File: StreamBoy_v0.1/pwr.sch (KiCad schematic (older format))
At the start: 4 parts

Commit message: Bunch of stuff
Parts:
- removed C1: 22uF/25V, Capacitor_SMD:C_0805_2012Metric, symbol Device:C
- removed C2: 0.1uF/50V, Capacitor_SMD:C_0805_2012Metric, symbol Device:C
- added C4, C? (x2): C, Capacitor_SMD:C_0805_2012Metric, symbol Device:C
- added D1, D2: D_Zener, b240a-13-f:DIOM5136X261N, symbol Device:D_Zener
- added L1, L2: INDUCTOR, Inductor_SMD:L_0805_2012Metric, symbol pspice:INDUCTOR
- added R43, R? (x3): R, Resistor_SMD:R_0805_2012Metric, symbol Device:R
- added U5, U6: TPS62170DSG, Package_SON:WSON-8-1EP_2x2mm_P0.5mm_EP0.9x1.6mm_ThermalVias, symbol Regulator_Switching:TPS62170DSG
- C3: value 0.1uF/50V -> C
- R1: value 10k -> R
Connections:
- net labels removed: GND
- wire segments 14 -> 0
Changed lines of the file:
@@
 Comment4 ""
 $EndDescr
+Text GLabel 9000 1550 2    50   Input ~ 0
+VCC3
+Text GLabel 9150 1950 2    50   Input ~ 0
+ESP_EN
 $Comp
-L Device:C C1
-U 1 1 5E0A08F0
-P 1550 1600
-F 0 "C1" H 1665 1646 50  0000 L CNN
-F 1 "22uF/25V" H 1665 1555 50  0000 L CNN
-F 2 "Capacitor_SMD:C_0805_2012Metric" H 1588 1450 50  0001 C CNN
-F 3 "~" H 1550 1600 50  0001 C CNN
-	1    1550 1600
+L Regulator_Switching:TPS62170DSG U6
+U 1 1 5E088ABF
+P 6900 1950
+F 0 "U6" H 6900 2517 50  0000 C CNN
+F 1 "TPS62170DSG" H 6900 2426 50  0000 C CNN
+F 2 "Package_SON:WSON-8-1EP_2x2mm_P0.5mm_EP0.9x1.6mm_ThermalVias" H 7050 1600 50  0001 L CNN
+F 3 "http://www.ti.com/lit/ds/symlink/tps62170.pdf" H 6900 2500 50  0001 C CNN
+	1    6900 1950
 	1    0    0    -1
 $EndComp
 $Comp
-L Device:C C2
-U 1 1 5E0A08F6
-P 1850 1400
-F 0 "C2" H 1965 1446 50  0000 L CNN
-F 1 "0.1uF/50V" H 1965 1355 50  0000 L CNN
-F 2 "Capacitor_SMD:C_0805_2012Metric" H 1888 1250 50  0001 C CNN
-F 3 "~" H 1850 1400 50  0001 C CNN
-	1    1850 1400
+L Regulator_Switching:TPS62170DSG U5
+U 1 1 5E08B4BD
+P 6850 3150
+F 0 "U5" H 6850 3717 50  0000 C CNN
+F 1 "TPS62170DSG" H 6850 3626 50  0000 C CNN
+F 2 "Package_SON:WSON-8-1EP_2x2mm_P0.5mm_EP0.9x1.6mm_ThermalVias" H 7000 2800 50  0001 L CNN
+F 3 "http://www.ti.com/lit/ds/symlink/tps62170.pdf" H 6850 3700 50  0001 C CNN
+	1    6850 3150
+	1    0    0    -1
+$EndComp
+$Comp
+L Device:D_Zener D1
+U 1 1 5E08BEF3
+P 5050 1750
+F 0 "D1" H 5050 1966 50  0000 C CNN
+F 1 "D_Zener" H 5050 1875 50  0000 C CNN
+F 2 "b240a-13-f:DIOM5136X261N" H 5050 1750 50  0001 C CNN
+F 3 "~" H 5050 1750 50  0001 C CNN
+	1    5050 1750
+	1    0    0    -1
+$EndComp
+$Comp
+L Device:D_Zener D2
+U 1 1 5E08C9DF
+P 5050 2150
+F 0 "D2" H 5050 2366 50  0000 C CNN
+F 1 "D_Zener" H 5050 2275 50  0000 C CNN
+F 2 "b240a-13-f:DIOM5136X261N" H 5050 2150 50  0001 C CNN
+F 3 "~" H 5050 2150 50  0001 C CNN
+	1    5050 2150
 	1    0    0    -1
 $EndComp
 $Comp
 L Device:C C3
-U 1 1 5E0A08FC
-P 2450 1950
-F 0 "C3" H 2565 1996 50  0000 L CNN
-F 1 "0.1uF/50V" H 2565 1905 50  0000 L CNN
-F 2 "Capacitor_SMD:C_0805_2012Metric" H 2488 1800 50  0001 C CNN
-F 3 "~" H 2450 1950 50  0001 C CNN
-	1    2450 1950
+U 1 1 5E08EF4C
+P 5600 2600
+F 0 "C3" H 5715 2646 50  0000 L CNN
+F 1 "C" H 5715 2555 50  0000 L CNN
+F 2 "Capacitor_SMD:C_0805_2012Metric" H 5638 2450 50  0001 C CNN
+F 3 "~" H 5600 2600 50  0001 C CNN
+	1    5600 2600
+	1    0    0    -1
+$EndComp
+$Comp
+L Device:C C4
+U 1 1 5E08F357
+P 5600 3300
+F 0 "C4" H 5715 3346 50  0000 L CNN
+F 1 "C" H 5715 3255 50  0000 L CNN
+F 2 "Capacitor_SMD:C_0805_2012Metric" H 5638 3150 50  0001 C CNN
+F 3 "~" H 5600 3300 50  0001 C CNN
+	1    5600 3300
+	1    0    0    -1
+$EndComp
+$Comp
+L Device:R R43
+U 1 1 5E08FF72
+P 5550 4100
+F 0 "R43" H 5620 4146 50  0000 L CNN
+F 1 "R" H 5620 4055 50  0000 L CNN
+F 2 "Resistor_SMD:R_0805_2012Metric" V 5480 4100 50  0001 C CNN
+F 3 "~" H 5550 4100 50  0001 C CNN
+	1    5550 4100
 	1    0    0    -1
 $EndComp
 $Comp
 L Device:R R1
-U 1 1 5E0A0902
-P 2450 1400
-F 0 "R1" H 2520 1446 50  0000 L CNN
-F 1 "10k" H 2520 1355 50  0000 L CNN
-F 2 "Resistor_SMD:R_0805_2012Metric" V 2380 1400 50  0001 C CNN
-F 3 "~" H 2450 1400 50  0001 C CNN
-	1    2450 1400
+U 1 1 5E09032D
+P 5300 4100
+F 0 "R1" H 5370 4146 50  0000 L CNN
+F 1 "R" H 5370 4055 50  0000 L CNN
+F 2 "Resistor_SMD:R_0805_2012Metric" V 5230 4100 50  0001 C CNN
+F 3 "~" H 5300 4100 50  0001 C CNN
+	1    5300 4100
 	1    0    0    -1
 $EndComp
 $Comp
-L power:GND #PWR0101
-U 1 1 5E0A0908
-P 1550 2200
-F 0 "#PWR0101" H 1550 1950 50  0001 C CNN
-F 1 "GND" H 1555 2027 50  0000 C CNN
-F 2 "" H 1550 2200 50  0001 C CNN
-F 3 "" H 1550 2200 50  0001 C CNN
-	1    1550 2200
+L pspice:INDUCTOR L1
+U 1 1 5E0929E5
+P 8600 1800
+F 0 "L1" H 8600 2015 50  0000 C CNN
+F 1 "INDUCTOR" H 8600 1924 50  0000 C CNN
+F 2 "Inductor_SMD:L_0805_2012Metric" H 8600 1800 50  0001 C CNN
+F 3 "~" H 8600 1800 50  0001 C CNN
+	1    8600 1800
 	1    0    0    -1
 $EndComp
 $Comp
-L power:GND #PWR0102
-U 1 1 5E0A090E
-P 2450 2250
-F 0 "#PWR0102" H 2450 2000 50  0001 C CNN
-F 1 "GND" H 2455 2077 50  0000 C CNN
-F 2 "" H 2450 2250 50  0001 C CNN
-F 3 "" H 2450 2250 50  0001 C CNN
-	1    2450 2250
+L pspice:INDUCTOR L2
+U 1 1 5E0933B4
+P 8600 2250
+F 0 "L2" H 8600 2465 50  0000 C CNN
+F 1 "INDUCTOR" H 8600 2374 50  0000 C CNN
+F 2 "Inductor_SMD:L_0805_2012Metric" H 8600 2250 50  0001 C CNN
+F 3 "~" H 8600 2250 50  0001 C CNN
+	1    8600 2250
 	1    0    0    -1
 $EndComp
-Text GLabel 1450 1050 0    50   Input ~ 0
-VCC3
-Wire Wire Line
-	1550 1050 1550 1450
-Connection ~ 1550 1050
-Wire Wire Line
-	1550 1050 1450 1050
-Wire Wire Line
-	1850 1050 1850 1250
-Connection ~ 1850 1050
-Wire Wire Line
-	1850 1050 1550 1050
-Wire Wire Line
-	1850 1550 1850 1950
-Wire Wire Line
-	1850 1950 1550 1950
-Wire Wire Line
-	1550 1950 1550 1750
-Wire Wire Line
-	1550 1950 1550 2200
-Connection ~ 1550 1950
-Wire Wire Line
-	2450 1550 2450 1700
-Wire Wire Line
-	2450 2100 2450 2250
-Wire Wire Line
-	2450 1250 2450 1050
-Wire Wire Line
-	2450 1050 1850 1050
-Text GLabel 2750 1700 2    50   Input ~ 0
-ESP_EN
-Wire Wire Line
-	2450 1700 2750 1700
-Connection ~ 2450 1700
-Wire Wire Line
-	2450 1700 2450 1800
+$Comp
+L Device:C C?
+U 1 1 5E0D4700
+P 4500 4100
+F 0 "C?" H 4615 4146 50  0000 L CNN
+F 1 "C" H 4615 4055 50  0000 L CNN
+F 2 "Capacitor_SMD:C_0805_2012Metric" H 4538 3950 50  0001 C CNN
+F 3 "~" H 4500 4100 50  0001 C CNN
+	1    4500 4100
+	1    0    0    -1
+$EndComp
+$Comp
+L Device:C C?
+U 1 1 5E0D4706
+P 4850 4100
+F 0 "C?" H 4965 4146 50  0000 L CNN
+F 1 "C" H 4965 4055 50  0000 L CNN
+F 2 "Capacitor_SMD:C_0805_2012Metric" H 4888 3950 50  0001 C CNN
+F 3 "~" H 4850 4100 50  0001 C CNN
+	1    4850 4100
+	1    0    0    -1
+$EndComp
+$Comp
+L Device:R R?
+U 1 1 5E0DEAFA
+P 6500 4150
+F 0 "R?" H 6570 4196 50  0000 L CNN
+F 1 "R" H 6570 4105 50  0000 L CNN
+F 2 "Resistor_SMD:R_0805_2012Metric" V 6430 4150 50  0001 C CNN
+F 3 "~" H 6500 4150 50  0001 C CNN
+	1    6500 4150
+	1    0    0    -1
+$EndComp
+$Comp
+L Device:R R?
+U 1 1 5E0DEB00
+P 6000 4150
+F 0 "R?" H 6070 4196 50  0000 L CNN
+F 1 "R" H 6070 4105 50  0000 L CNN
+F 2 "Resistor_SMD:R_0805_2012Metric" V 5930 4150 50  0001 C CNN
+F 3 "~" H 6000 4150 50  0001 C CNN
+	1    6000 4150
+	1    0    0    -1
+$EndComp
+$Comp
+L Device:R R?
+U 1 1 5E0DEB06
+P 6900 4150
+F 0 "R?" H 6970 4196 50  0000 L CNN
+F 1 "R" H 6970 4105 50  0000 L CNN
+F 2 "Resistor_SMD:R_0805_2012Metric" V 6830 4150 50  0001 C CNN
+F 3 "~" H 6900 4150 50  0001 C CNN
+	1    6900 4150
+	1    0    0    -1
+$EndComp
 $EndSCHEMATC

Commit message: Power to the masses
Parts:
- removed C3, C4: C, Capacitor_SMD:C_0805_2012Metric, symbol Device:C
- removed D1, D2: D_Zener, b240a-13-f:DIOM5136X261N, symbol Device:D_Zener
- removed R1, R43: R, Resistor_SMD:R_0805_2012Metric, symbol Device:R
- removed U5: TPS62170DSG, Package_SON:WSON-8-1EP_2x2mm_P0.5mm_EP0.9x1.6mm_ThermalVias, symbol Regulator_Switching:TPS62170DSG
- added C5: 10uF, Capacitor_SMD:C_0805_2012Metric, symbol Device:C
- added C6: 22uF, Capacitor_SMD:C_0805_2012Metric, symbol Device:C
- added D1, D2: D, Diode_SMD:D_0805_2012Metric, symbol Device:D
- added R4: 75KOhm, Resistor_SMD:R_0805_2012Metric, symbol Device:R
- added R7: 24KOhm, Resistor_SMD:R_0805_2012Metric, symbol Device:R
- added U7: TPS62170DSG, Package_SON:WSON-8-1EP_2x2mm_P0.5mm_EP0.9x1.6mm_ThermalVias, symbol Regulator_Switching:TPS62170DSG
- C3: renamed from C?; value C -> 22uF
- C4: renamed from C?; value C -> 10uF
- L1, L2: value INDUCTOR -> 2.2uH
- R1: renamed from R?; value R -> 75KOhm
- R2: renamed from R?; value R -> 24KOhm
- R3: renamed from R?; value R -> 100KOhm
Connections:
- net labels added: GB_5V, GND, USB5V, VCC1V2, VCC5
- wire segments 0 -> 65
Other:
- moved on the sheet: C3, C4, L1, R1, R2, R3

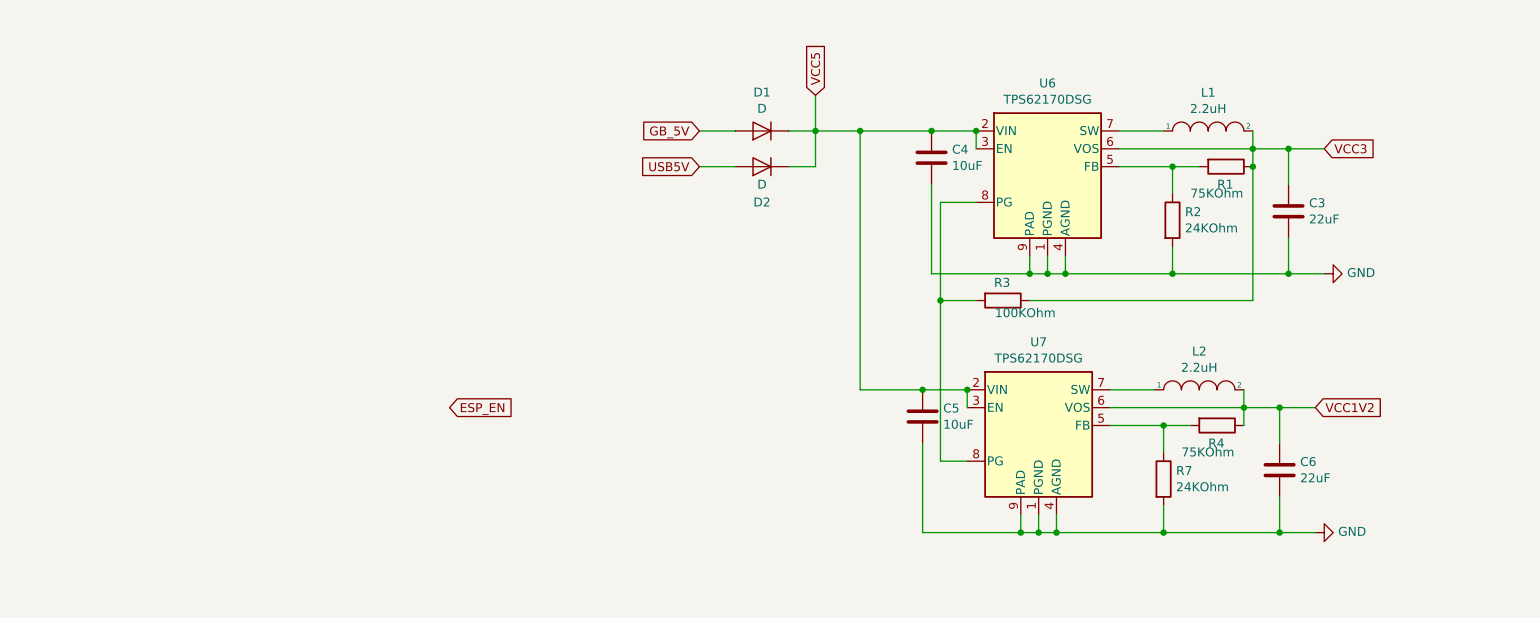
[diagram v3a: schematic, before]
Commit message: Fix one resistor in pwr
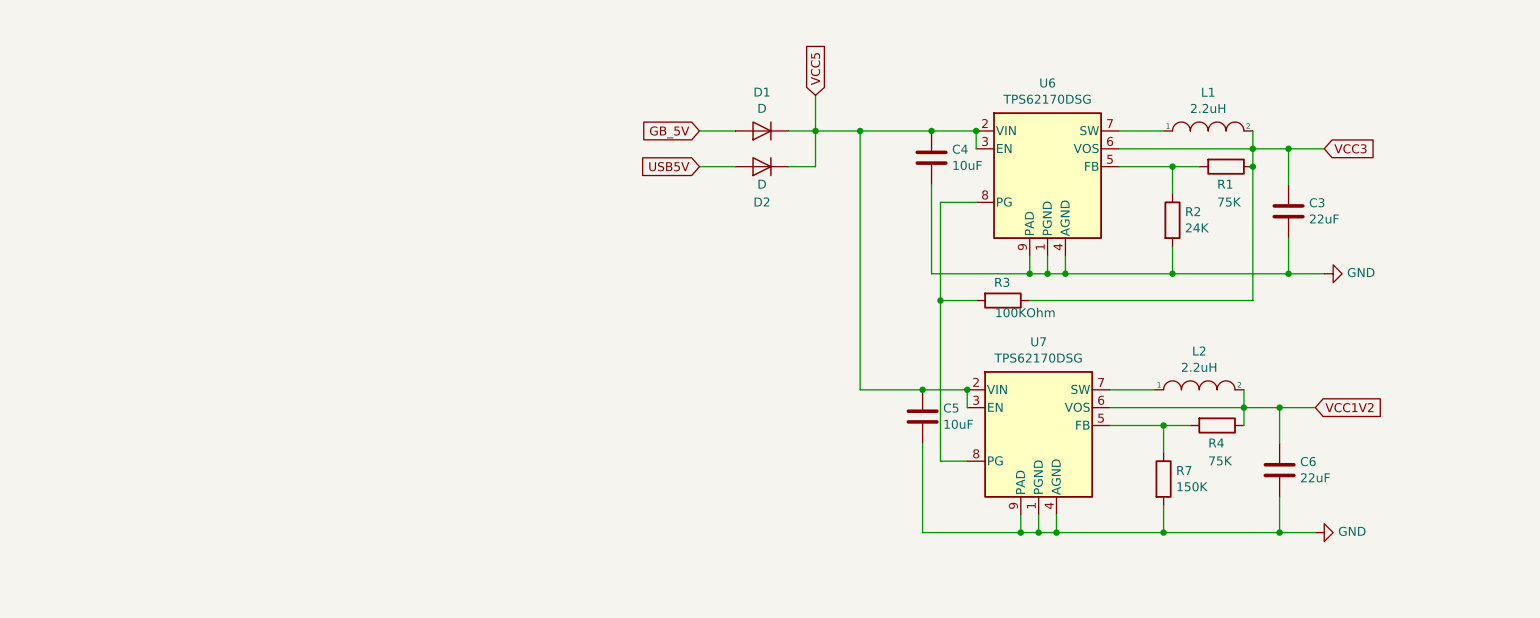
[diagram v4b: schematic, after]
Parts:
- R1, R4: value 75KOhm -> 75K
- R2: value 24KOhm -> 24K
- R7: value 24KOhm -> 150K
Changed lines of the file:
@@
 EESchema Schematic File Version 4
-EELAYER 30 0
+LIBS:StreamBoy-cache
+EELAYER 29 0
 EELAYER END
 $Descr A4 11693 8268
@@
 Comment4 ""
 $EndDescr
-Text GLabel 3550 3200 2    50   Input ~ 0
-ESP_EN
 $Comp
 L Regulator_Switching:TPS62170DSG U6
@@
 P 7600 2150
 F 0 "R2" H 7670 2196 50  0000 L CNN
-F 1 "24KOhm" H 7670 2105 50  0000 L CNN
+F 1 "24K" H 7670 2105 50  0000 L CNN
 F 2 "Resistor_SMD:R_0805_2012Metric" V 7530 2150 50  0001 C CNN
 F 3 "~" H 7600 2150 50  0001 C CNN
@@
 P 7900 1850
 F 0 "R1" V 8000 1800 50  0000 L CNN
-F 1 "75KOhm" V 8050 1650 50  0000 L CNN
+F 1 "75K" V 8100 1800 50  0000 L CNN
 F 2 "Resistor_SMD:R_0805_2012Metric" V 7830 1850 50  0001 C CNN
 F 3 "~" H 7900 1850 50  0001 C CNN
@@
 Connection ~ 7600 2450
 $Comp
-L power:GND #PWR?
+L power:GND #PWR0113
 U 1 1 5E11504D
 P 8450 2450
-F 0 "#PWR?" H 8450 2200 50  0001 C CNN
+F 0 "#PWR0113" H 8450 2200 50  0001 C CNN
 F 1 "GND" V 8455 2322 50  0000 R CNN
 F 2 "" H 8450 2450 50  0001 C CNN
@@
 P 7550 3600
 F 0 "R7" H 7620 3646 50  0000 L CNN
-F 1 "24KOhm" H 7620 3555 50  0000 L CNN
+F 1 "150K" H 7620 3555 50  0000 L CNN
 F 2 "Resistor_SMD:R_0805_2012Metric" V 7480 3600 50  0001 C CNN
 F 3 "~" H 7550 3600 50  0001 C CNN
@@
 P 7850 3300
 F 0 "R4" V 7950 3250 50  0000 L CNN
-F 1 "75KOhm" V 8000 3100 50  0000 L CNN
+F 1 "75K" V 8050 3250 50  0000 L CNN
 F 2 "Resistor_SMD:R_0805_2012Metric" V 7780 3300 50  0001 C CNN
 F 3 "~" H 7850 3300 50  0001 C CNN
@@
 Connection ~ 7550 3900
 $Comp
-L power:GND #PWR?
+L power:GND #PWR0114
 U 1 1 5E11E11B
 P 8400 3900
-F 0 "#PWR?" H 8400 3650 50  0001 C CNN
+F 0 "#PWR0114" H 8400 3650 50  0001 C CNN
 F 1 "GND" V 8405 3772 50  0000 R CNN
 F 2 "" H 8400 3900 50  0001 C CNN

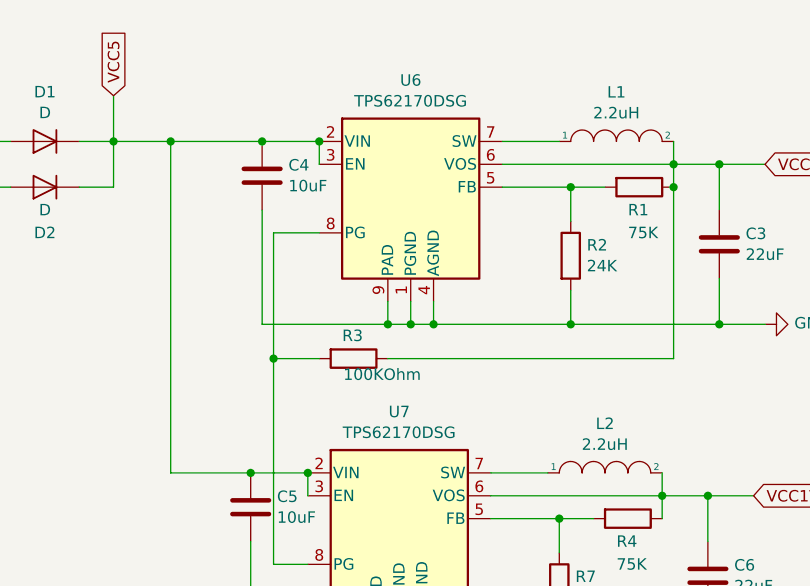
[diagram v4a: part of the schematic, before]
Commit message: Update some labels
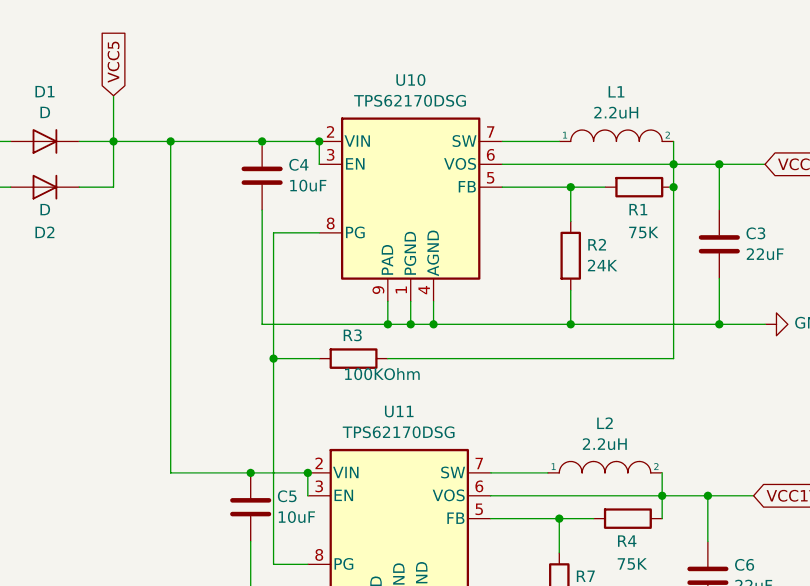
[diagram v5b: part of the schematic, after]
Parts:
- renumbered U6 to U10, U7 to U11
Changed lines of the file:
@@
 $EndDescr
 $Comp
-L Regulator_Switching:TPS62170DSG U6
+L Regulator_Switching:TPS62170DSG U10
 U 1 1 5E088ABF
 P 6900 1950
-F 0 "U6" H 6900 2517 50  0000 C CNN
+F 0 "U10" H 6900 2517 50  0000 C CNN
 F 1 "TPS62170DSG" H 6900 2426 50  0000 C CNN
 F 2 "Package_SON:WSON-8-1EP_2x2mm_P0.5mm_EP0.9x1.6mm_ThermalVias" H 7050 1600 50  0001 L CNN
@@
 Connection ~ 6800 2450
 $Comp
-L Regulator_Switching:TPS62170DSG U7
+L Regulator_Switching:TPS62170DSG U11
 U 1 1 5E11E0DE
 P 6850 3400
-F 0 "U7" H 6850 3967 50  0000 C CNN
+F 0 "U11" H 6850 3967 50  0000 C CNN
 F 1 "TPS62170DSG" H 6850 3876 50  0000 C CNN
 F 2 "Package_SON:WSON-8-1EP_2x2mm_P0.5mm_EP0.9x1.6mm_ThermalVias" H 7000 3050 50  0001 L CNN

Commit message: I hate component placement!
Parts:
- C3, C6: footprint Capacitor_SMD:C_0805_2012Metric -> Capacitor_SMD:C_0603_1608Metric; lcscPartnum (none) -> C59461
- C4, C5: footprint Capacitor_SMD:C_0805_2012Metric -> Capacitor_SMD:C_0402_1005Metric; lcscPartnum (none) -> C15525
- L1, L2: lcscPartnum (none) -> C1043
- R1, R4: footprint Resistor_SMD:R_0805_2012Metric -> Resistor_SMD:R_0402_1005Metric; lcscPartnum (none) -> C25798
- R2: footprint Resistor_SMD:R_0805_2012Metric -> Resistor_SMD:R_0402_1005Metric; lcscPartnum (none) -> C25769
- R3: footprint Resistor_SMD:R_0805_2012Metric -> Resistor_SMD:R_0402_1005Metric; lcscPartnum (none) -> C25741
- R7: footprint Resistor_SMD:R_0805_2012Metric -> Resistor_SMD:R_0402_1005Metric; lcscPartnum (none) -> C25755
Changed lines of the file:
@@
 EESchema Schematic File Version 4
-LIBS:StreamBoy-cache
-EELAYER 29 0
+EELAYER 30 0
 EELAYER END
 $Descr A4 11693 8268
@@
 F 2 "Inductor_SMD:L_0805_2012Metric" H 7800 1650 50  0001 C CNN
 F 3 "~" H 7800 1650 50  0001 C CNN
+F 4 "C1043" H 7800 1650 50  0001 C CNN "lcscPartnum"
 	1    7800 1650
 	1    0    0    -1
@@
 F 0 "C4" H 6365 1846 50  0000 L CNN
 F 1 "10uF" H 6365 1755 50  0000 L CNN
-F 2 "Capacitor_SMD:C_0805_2012Metric" H 6288 1650 50  0001 C CNN
+F 2 "Capacitor_SMD:C_0402_1005Metric" H 6288 1650 50  0001 C CNN
 F 3 "~" H 6250 1800 50  0001 C CNN
+F 4 "C15525" H 6250 1800 50  0001 C CNN "lcscPartnum"
 	1    6250 1800
 	1    0    0    -1
@@
 F 0 "C3" H 8365 2146 50  0000 L CNN
 F 1 "22uF" H 8365 2055 50  0000 L CNN
-F 2 "Capacitor_SMD:C_0805_2012Metric" H 8288 1950 50  0001 C CNN
+F 2 "Capacitor_SMD:C_0603_1608Metric" H 8288 1950 50  0001 C CNN
 F 3 "~" H 8250 2100 50  0001 C CNN
+F 4 "C59461" H 8250 2100 50  0001 C CNN "lcscPartnum"
 	1    8250 2100
 	1    0    0    -1
@@
 F 0 "R2" H 7670 2196 50  0000 L CNN
 F 1 "24K" H 7670 2105 50  0000 L CNN
-F 2 "Resistor_SMD:R_0805_2012Metric" V 7530 2150 50  0001 C CNN
+F 2 "Resistor_SMD:R_0402_1005Metric" V 7530 2150 50  0001 C CNN
 F 3 "~" H 7600 2150 50  0001 C CNN
+F 4 "C25769" H 7600 2150 50  0001 C CNN "lcscPartnum"
 	1    7600 2150
 	1    0    0    -1
@@
 F 0 "R3" V 6550 2550 50  0000 L CNN
 F 1 "100KOhm" V 6720 2555 50  0000 L CNN
-F 2 "Resistor_SMD:R_0805_2012Metric" V 6580 2600 50  0001 C CNN
+F 2 "Resistor_SMD:R_0402_1005Metric" V 6580 2600 50  0001 C CNN
 F 3 "~" H 6650 2600 50  0001 C CNN
+F 4 "C25741" H 6650 2600 50  0001 C CNN "lcscPartnum"
 	1    6650 2600
 	0    1    1    0
@@
 F 0 "R1" V 8000 1800 50  0000 L CNN
 F 1 "75K" V 8100 1800 50  0000 L CNN
-F 2 "Resistor_SMD:R_0805_2012Metric" V 7830 1850 50  0001 C CNN
+F 2 "Resistor_SMD:R_0402_1005Metric" V 7830 1850 50  0001 C CNN
 F 3 "~" H 7900 1850 50  0001 C CNN
+F 4 "C25798" H 7900 1850 50  0001 C CNN "lcscPartnum"
 	1    7900 1850
 	0    1    1    0
@@
 F 2 "Inductor_SMD:L_0805_2012Metric" H 7750 3100 50  0001 C CNN
 F 3 "~" H 7750 3100 50  0001 C CNN
+F 4 "C1043" H 7750 3100 50  0001 C CNN "lcscPartnum"
 	1    7750 3100
 	1    0    0    -1
@@
 F 0 "C5" H 6315 3296 50  0000 L CNN
 F 1 "10uF" H 6315 3205 50  0000 L CNN
-F 2 "Capacitor_SMD:C_0805_2012Metric" H 6238 3100 50  0001 C CNN
+F 2 "Capacitor_SMD:C_0402_1005Metric" H 6238 3100 50  0001 C CNN
 F 3 "~" H 6200 3250 50  0001 C CNN
+F 4 "C15525" H 6200 3250 50  0001 C CNN "lcscPartnum"
 	1    6200 3250
 	1    0    0    -1
@@
 F 0 "C6" H 8315 3596 50  0000 L CNN
 F 1 "22uF" H 8315 3505 50  0000 L CNN
-F 2 "Capacitor_SMD:C_0805_2012Metric" H 8238 3400 50  0001 C CNN
+F 2 "Capacitor_SMD:C_0603_1608Metric" H 8238 3400 50  0001 C CNN
 F 3 "~" H 8200 3550 50  0001 C CNN
+F 4 "C59461" H 8200 3550 50  0001 C CNN "lcscPartnum"
 	1    8200 3550
-	1    0    0    -1
-$EndComp
-$Comp
-L Device:R R7
-U 1 1 5E11E0F6
-P 7550 3600
-F 0 "R7" H 7620 3646 50  0000 L CNN
-F 1 "150K" H 7620 3555 50  0000 L CNN
-F 2 "Resistor_SMD:R_0805_2012Metric" V 7480 3600 50  0001 C CNN
-F 3 "~" H 7550 3600 50  0001 C CNN
-	1    7550 3600
 	1    0    0    -1
 $EndComp
@@
 F 0 "R4" V 7950 3250 50  0000 L CNN
 F 1 "75K" V 8050 3250 50  0000 L CNN
-F 2 "Resistor_SMD:R_0805_2012Metric" V 7780 3300 50  0001 C CNN
+F 2 "Resistor_SMD:R_0402_1005Metric" V 7780 3300 50  0001 C CNN
 F 3 "~" H 7850 3300 50  0001 C CNN
+F 4 "C25798" V 7850 3300 50  0001 C CNN "lcscPartnum"
 	1    7850 3300
 	0    1    1    0
@@
 Text GLabel 4950 1650 0    50   Input ~ 0
 GB_5V
+$Comp
+L Device:R R7
+U 1 1 5E11E0F6
+P 7550 3600
+F 0 "R7" H 7620 3646 50  0000 L CNN
+F 1 "150K" H 7620 3555 50  0000 L CNN
+F 2 "Resistor_SMD:R_0402_1005Metric" V 7480 3600 50  0001 C CNN
+F 3 "~" H 7550 3600 50  0001 C CNN
+F 4 "C25755" H 7550 3600 50  0001 C CNN "lcscPartnum"
+	1    7550 3600
+	1    0    0    -1
+$EndComp
 $EndSCHEMATC

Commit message: Started to route some stuff
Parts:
- D1, D2: footprint Diode_SMD:D_0805_2012Metric -> Diode_SMD:D_SOD-123F; lcscPartnum (none) -> C64898
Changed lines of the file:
@@
 F 0 "D1" H 5300 1434 50  0000 C CNN
 F 1 "D" H 5300 1525 50  0000 C CNN
-F 2 "Diode_SMD:D_0805_2012Metric" H 5300 1650 50  0001 C CNN
+F 2 "Diode_SMD:D_SOD-123F" H 5300 1650 50  0001 C CNN
 F 3 "~" H 5300 1650 50  0001 C CNN
+F 4 "C64898" H 5300 1650 50  0001 C CNN "lcscPartnum"
 	1    5300 1650
 	-1   0    0    1
@@
 F 0 "D2" H 5300 2050 50  0000 C CNN
 F 1 "D" H 5300 1950 50  0000 C CNN
-F 2 "Diode_SMD:D_0805_2012Metric" H 5300 1850 50  0001 C CNN
+F 2 "Diode_SMD:D_SOD-123F" H 5300 1850 50  0001 C CNN
 F 3 "~" H 5300 1850 50  0001 C CNN
+F 4 "C64898" H 5300 1850 50  0001 C CNN "lcscPartnum"
 	1    5300 1850
 	-1   0    0    1
